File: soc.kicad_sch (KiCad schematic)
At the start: 89 parts, among them U1 MPFS250T-FCVG484

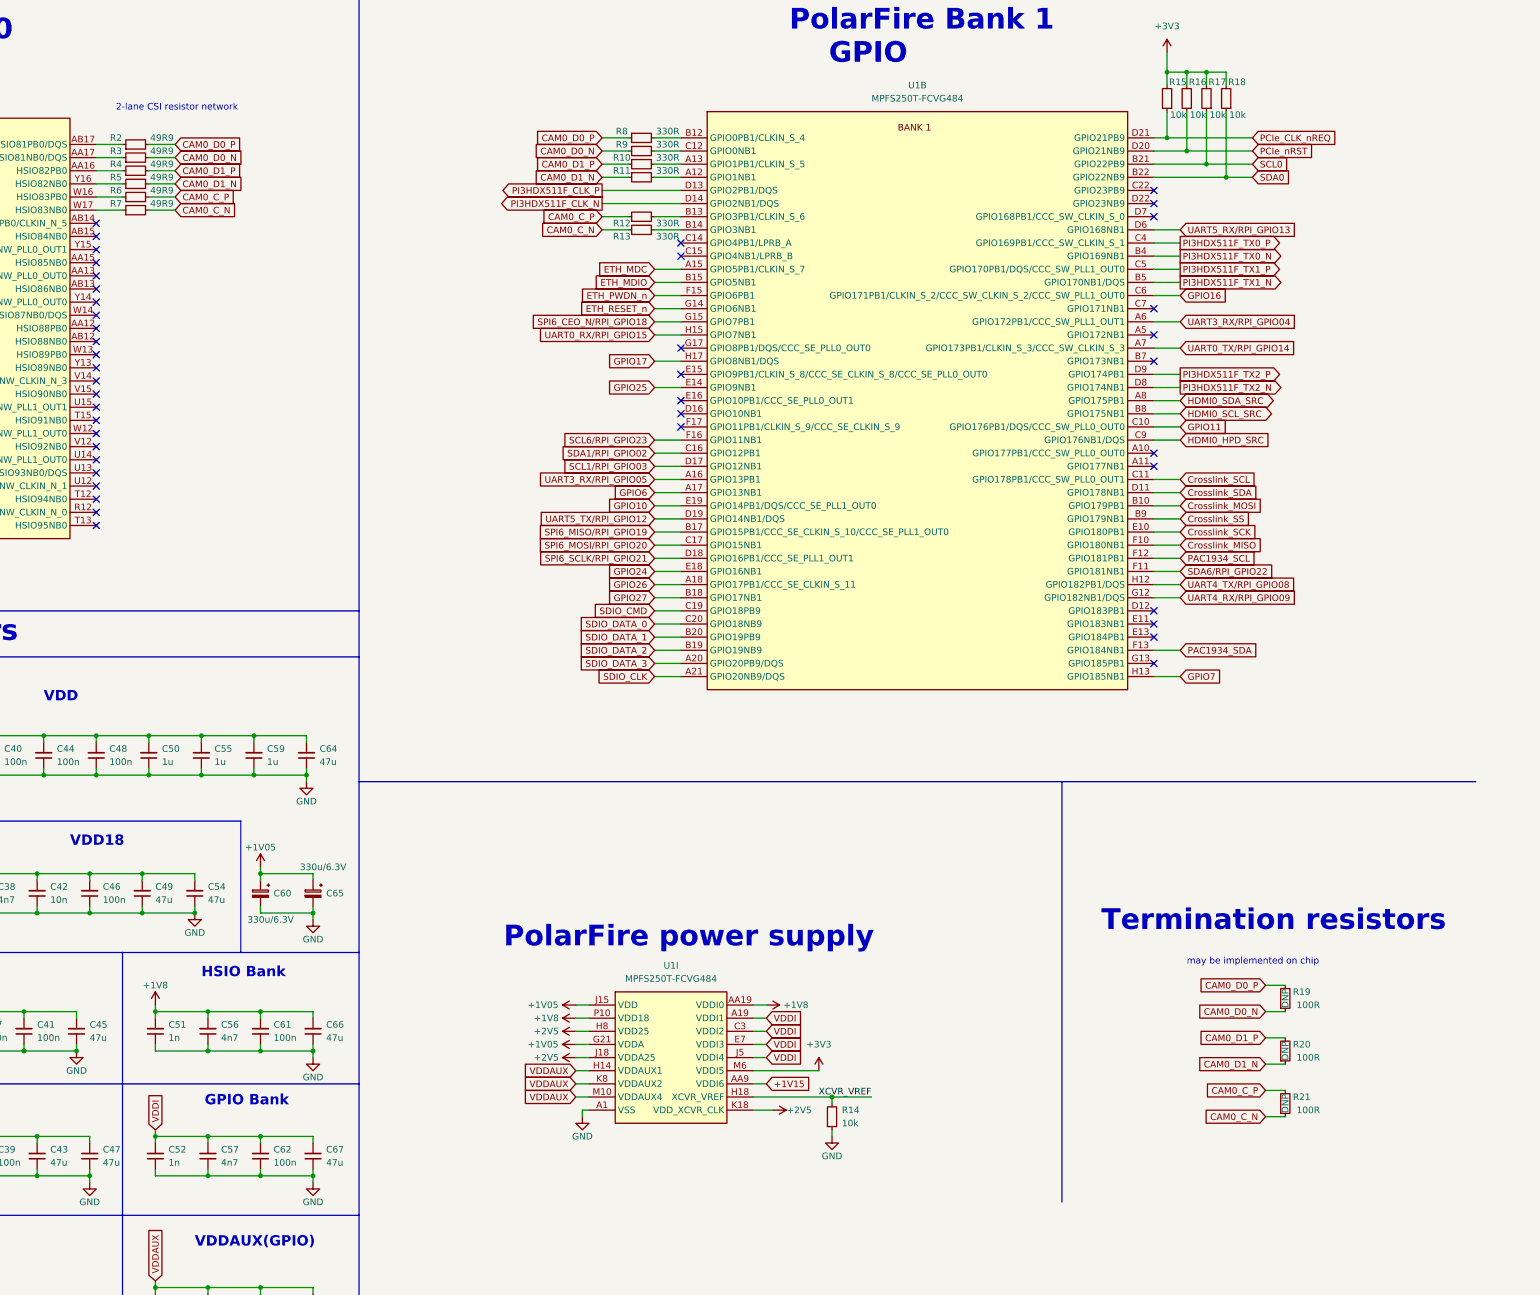
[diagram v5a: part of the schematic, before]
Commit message: [#55275] Implement MIPI on GPIO
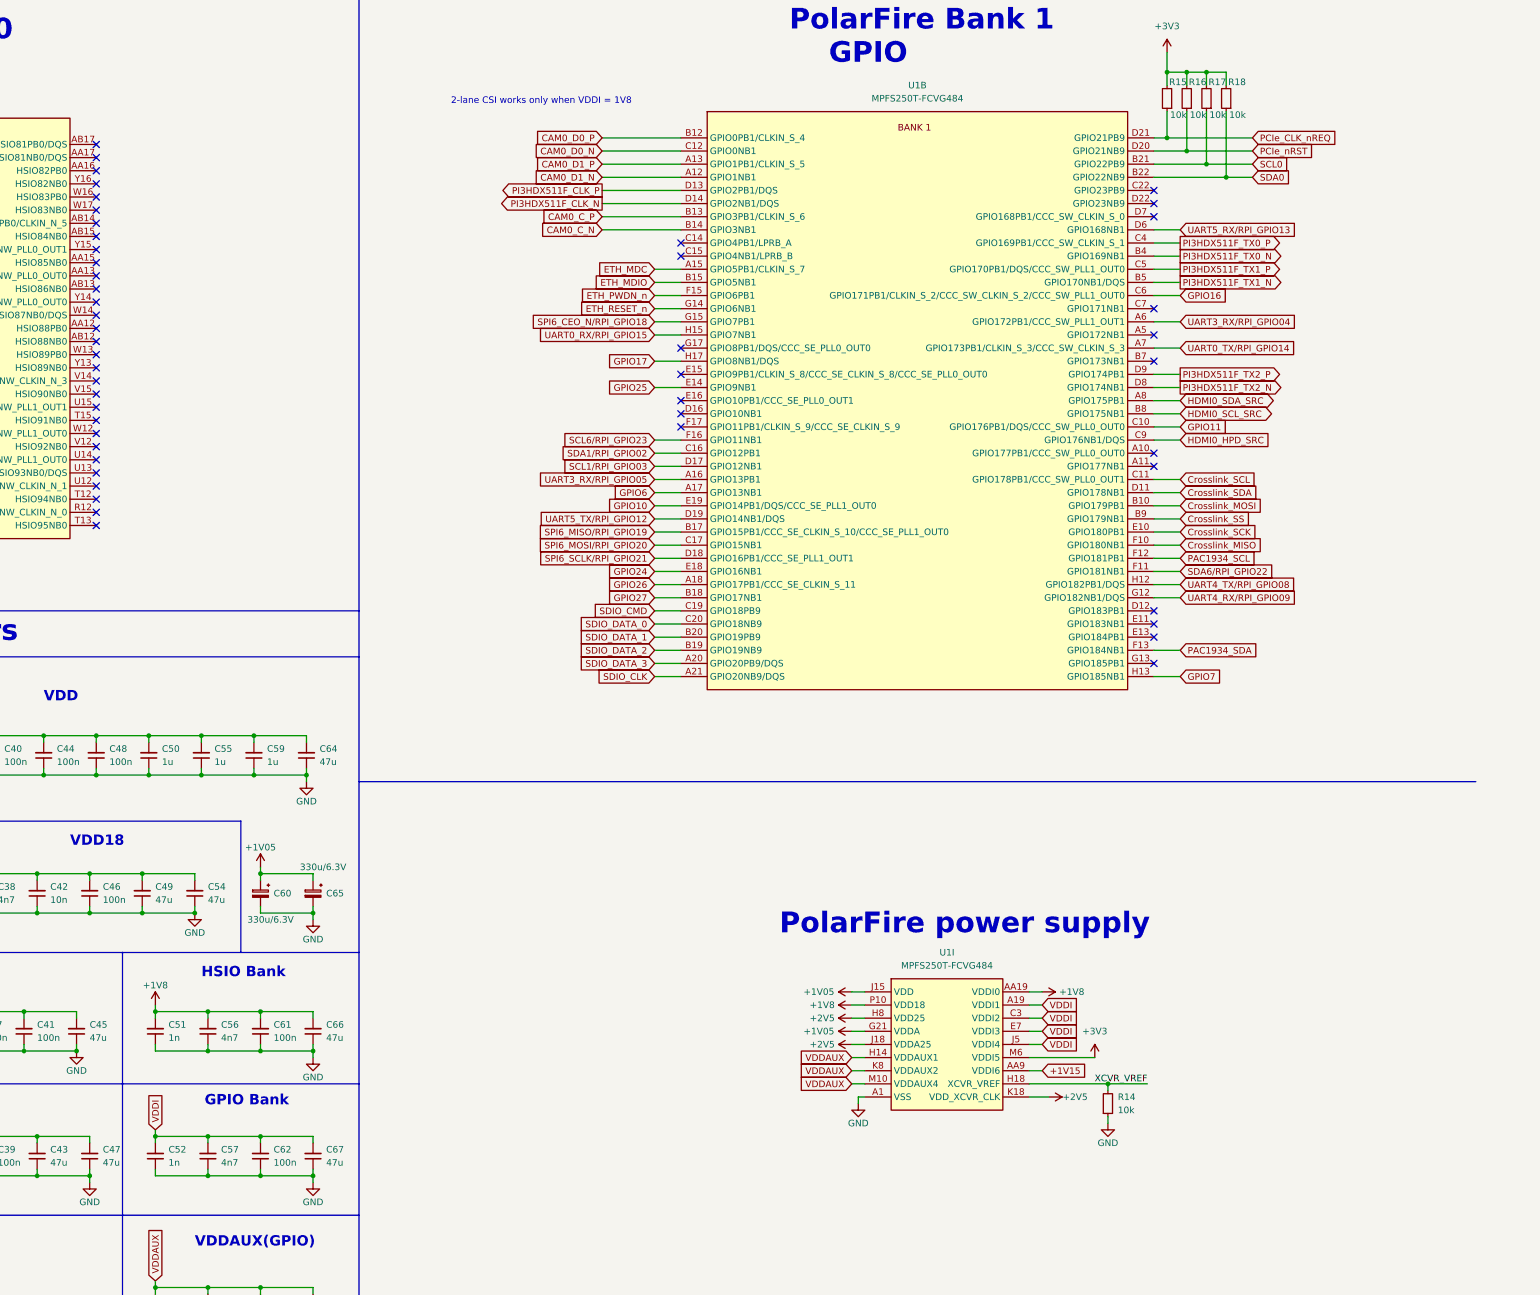
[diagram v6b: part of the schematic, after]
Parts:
- removed R10, R11, R12, R13, R8, R9: R_330R_0402, antmicro-footprints:R_0402_1005Metric, symbol antmicroResistors0402:R_330R_0402
- removed R19, R20, R21: R_100R_0402, antmicro-footprints:R_0402_1005Metric, symbol antmicroResistors0402:R_100R_0402
- removed R2, R3, R4, R5, R6, R7: R_49R9_0402, antmicro-footprints:R_0402_1005Metric, symbol antmicroResistors0402:R_49R9_0402
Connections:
- net CAM0_C_N: now also U1.B14 (GPIO3NB1)
- net CAM0_C_P: now also U1.B13 (GPIO3PB1/CLKIN_S_6)
- net CAM0_D0_N: now also U1.C12 (GPIO0NB1)
- net CAM0_D0_P: now also U1.B12 (GPIO0PB1/CLKIN_S_4)
- net CAM0_D1_N: now also U1.A12 (GPIO1NB1)
- net CAM0_D1_P: now also U1.A13 (GPIO1PB1/CLKIN_S_5)
- no-connect marks 49 -> 55
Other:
- note added: "2-lane CSI works only when VDDI = 1V8"
- note removed: "2-lane CSI resistor network"
- note removed: "Termination resistors"
- note removed: "may be implemented on chip"
- moved on the sheet: R14, U1I

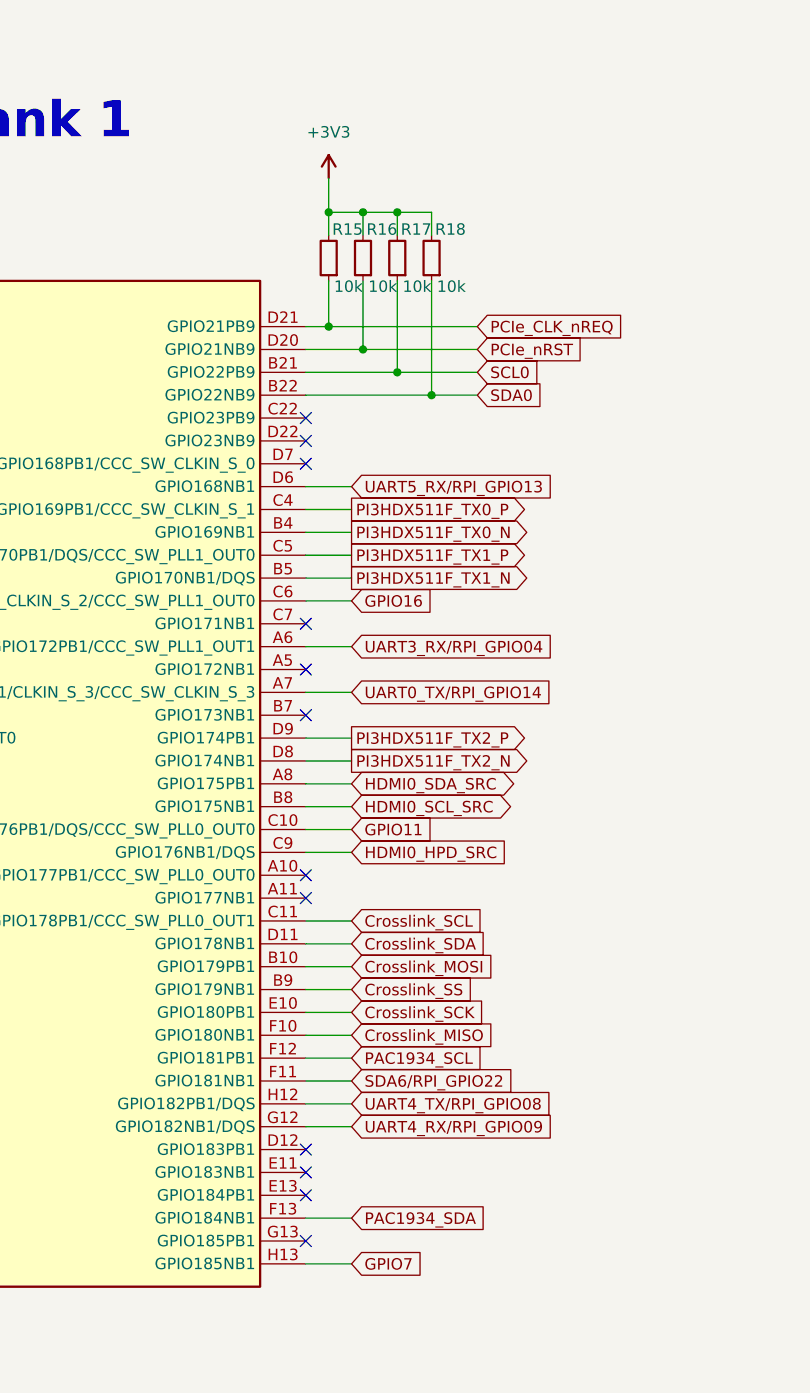
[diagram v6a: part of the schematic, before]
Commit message: [#54899] Change ETH labels to differential
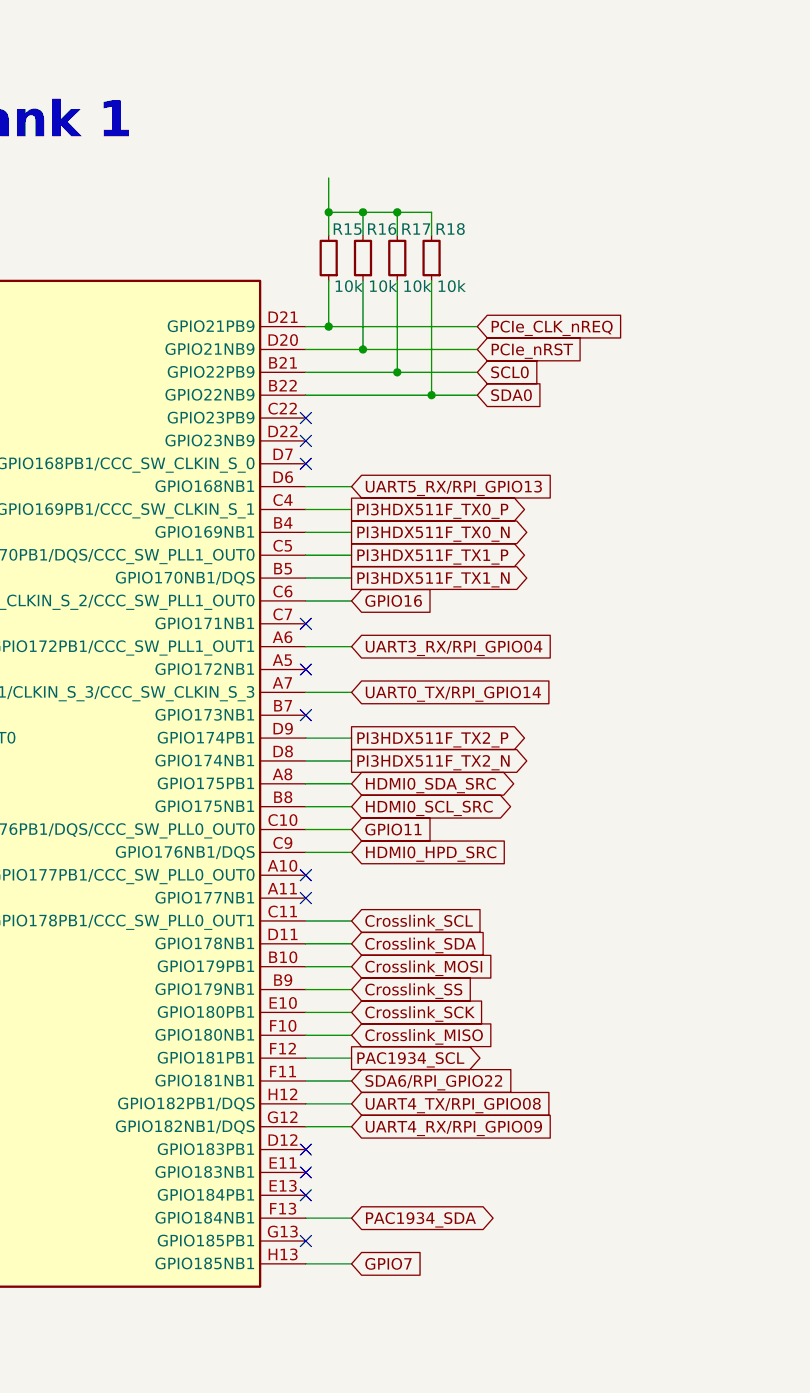
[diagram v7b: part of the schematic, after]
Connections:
- net +3V3: no longer R15.2, R16.2, R17.2, R18.2
- new net: R15.2, R16.2, R17.2, R18.2
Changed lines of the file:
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@@
     )
   )
-  (global_label "PAC1934_SDA" (shape input) (at 350.52 146.05 0) (fields_autoplaced)
+  (global_label "PAC1934_SDA" (shape bidirectional) (at 350.52 146.05 0) (fields_autoplaced)
     (effects (font (size 1.27 1.27)) (justify left))
-    (property "Intersheetrefs" "${INTERSHEET_REFS}" (at 365.9355 145.9706 0)
+    (property "Intersheetrefs" "${INTERSHEET_REFS}" (at 367.6188 146.05 0)
       (effects (font (size 1.27 1.27)) (justify left) hide)
     )
@@
     )
   )
-  (global_label "PAC1934_SCL" (shape input) (at 350.52 128.27 0) (fields_autoplaced)
+  (global_label "PAC1934_SCL" (shape output) (at 350.52 128.27 0) (fields_autoplaced)
     (effects (font (size 1.27 1.27)) (justify left))
-    (property "Intersheetrefs" "${INTERSHEET_REFS}" (at 365.875 128.1906 0)
+    (property "Intersheetrefs" "${INTERSHEET_REFS}" (at 366.447 128.27 0)
       (effects (font (size 1.27 1.27)) (justify left) hide)
     )
@@
         )
       )
-    )
-  )
-  (symbol (lib_id "antmicropower:+3V3") (at 347.98 30.48 0) (unit 1)
-    (in_bom yes) (on_board yes) (dnp no) (fields_autoplaced)
-    (property "Reference" "#PWR045" (at 363.22 33.02 0)
-      (effects (font (size 1.27 1.27) (thickness 0.15)) (justify left bottom) hide)
-    )
-    (property "Value" "+3V3" (at 347.98 25.4 0)
-      (effects (font (size 1.27 1.27) (thickness 0.15)))
-    )
-    (property "Footprint" "" (at 363.22 38.1 0)
-      (effects (font (size 1.27 1.27) (thickness 0.15)) (justify left bottom) hide)
-    )
-    (property "Datasheet" "" (at 363.22 40.64 0)
-      (effects (font (size 1.27 1.27) (thickness 0.15)) (justify left bottom) hide)
-    )
-    (property "Author" "Antmicro" (at 363.22 38.1 0)
-      (effects (font (size 1.27 1.27) (thickness 0.15)) (justify left bottom) hide)
-    )
-    (property "License" "Apache-2.0" (at 363.22 40.64 0)
-      (effects (font (size 1.27 1.27) (thickness 0.15)) (justify left bottom) hide)
-    )
-    (pin "1")
-    (instances
-      (project "polarfire-som"
-        (path "/db4a0d3e-2eb3-499e-977d-6eb378cfd3ed/99f116ae-bc8e-42a5-8f88-aecc401b3bcc"
-          (reference "#PWR045") (unit 1)
-        )
-      )

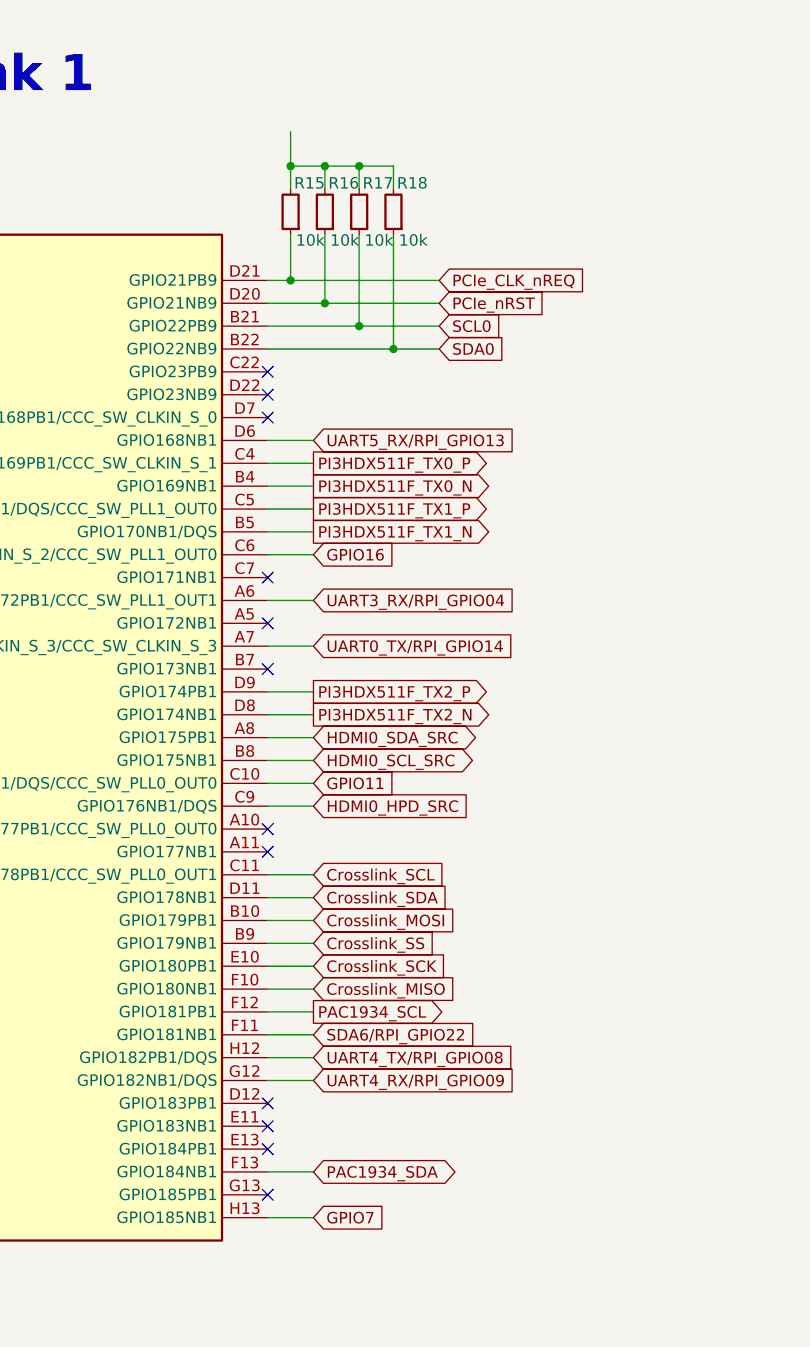
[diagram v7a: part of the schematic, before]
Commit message: [#55285] Add I2C0 level converter
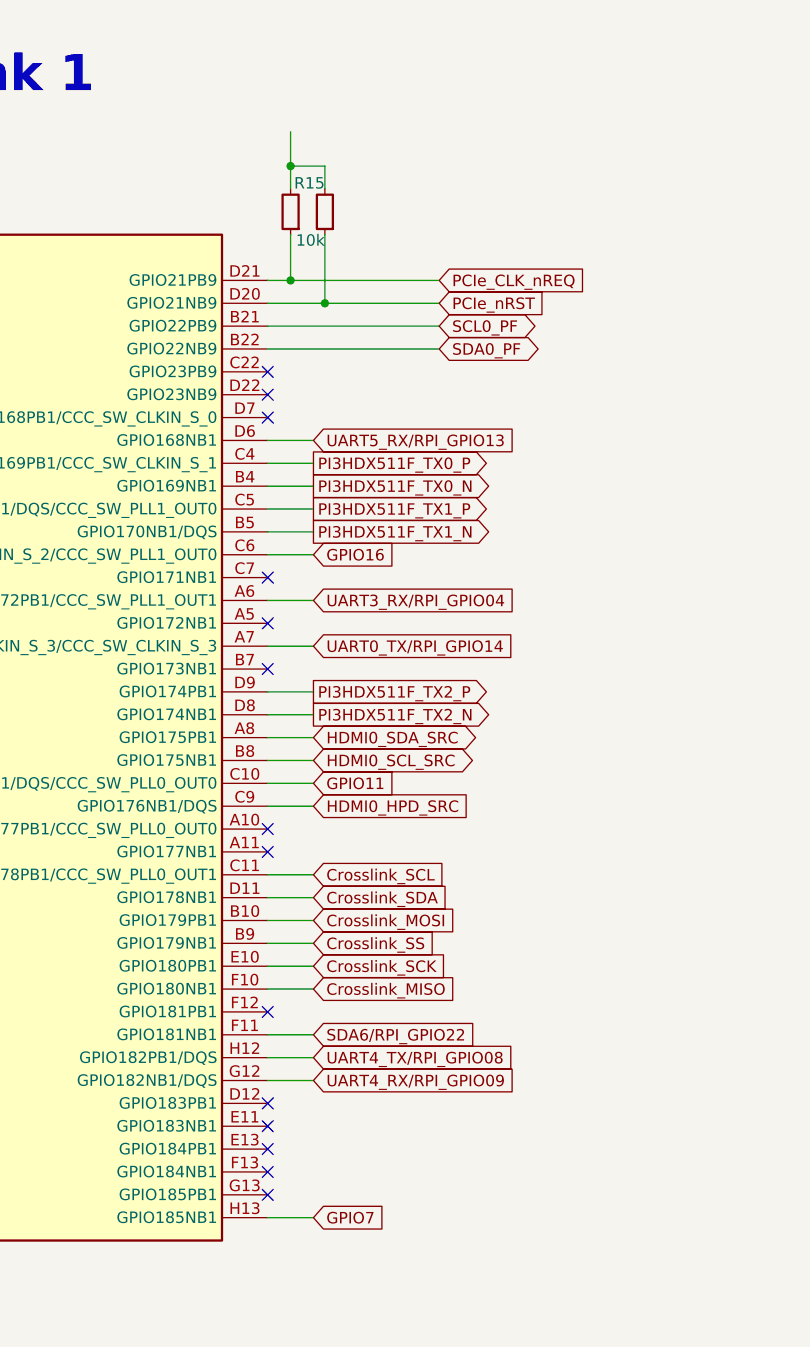
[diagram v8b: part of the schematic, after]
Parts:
- removed R17, R18: R_10k_0402, antmicro-footprints:R_0402_1005Metric, symbol antmicroResistors0402:R_10k_0402
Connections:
- net PAC1934_SCL: no longer names the net of U1.F12 (GPIO181PB1)
- net PAC1934_SDA: no longer names the net of U1.F13 (GPIO184NB1)
- net SCL0 renamed SCL0_PF
- net SDA0 renamed SDA0_PF
- no-connect marks 55 -> 57
